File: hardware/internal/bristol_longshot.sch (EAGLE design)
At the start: 39 parts, among them U1 SAM_D20E, U15 BMP180, U2 SI4060, U7 TPS3123, U8 SN74LVC1G32DCKR

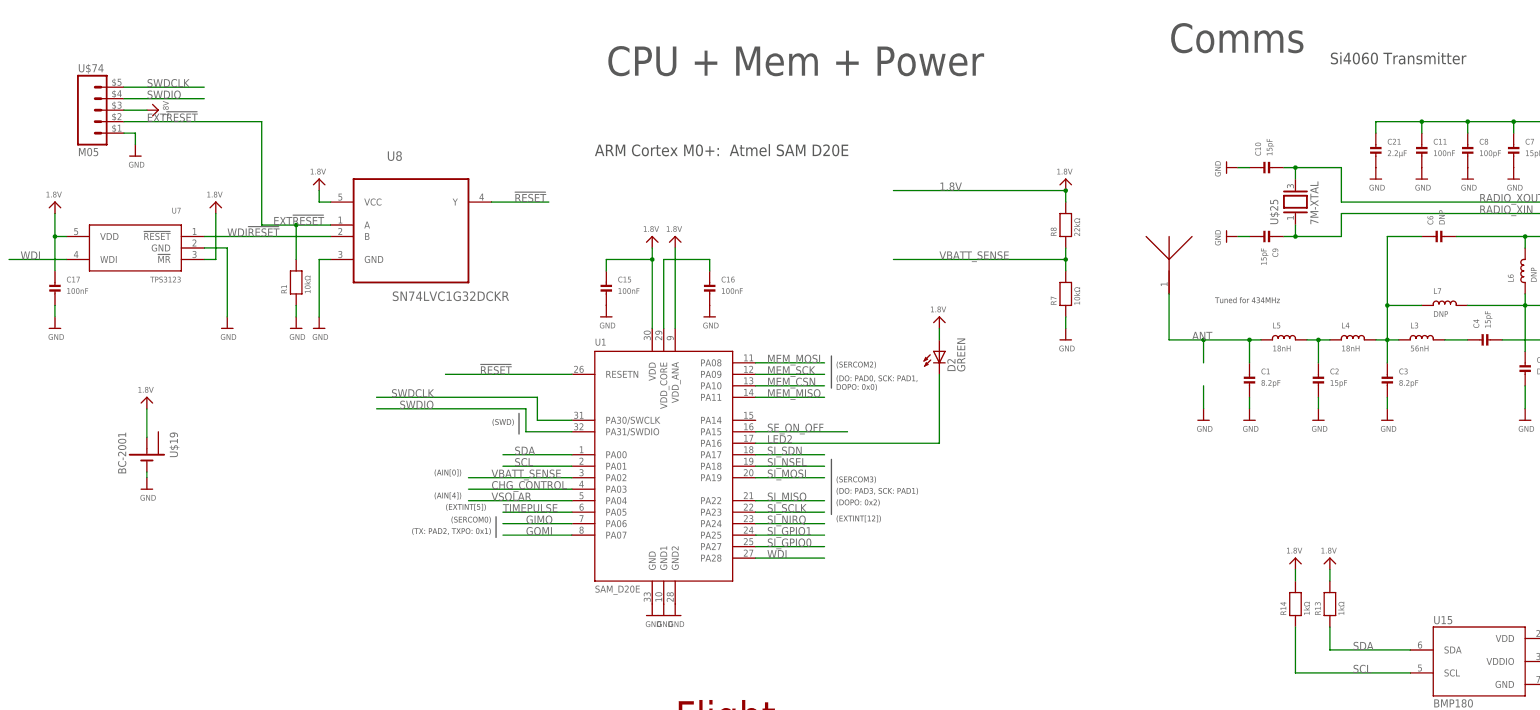
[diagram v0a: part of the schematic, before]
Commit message: Updated main solar active components names to correspond with partslist
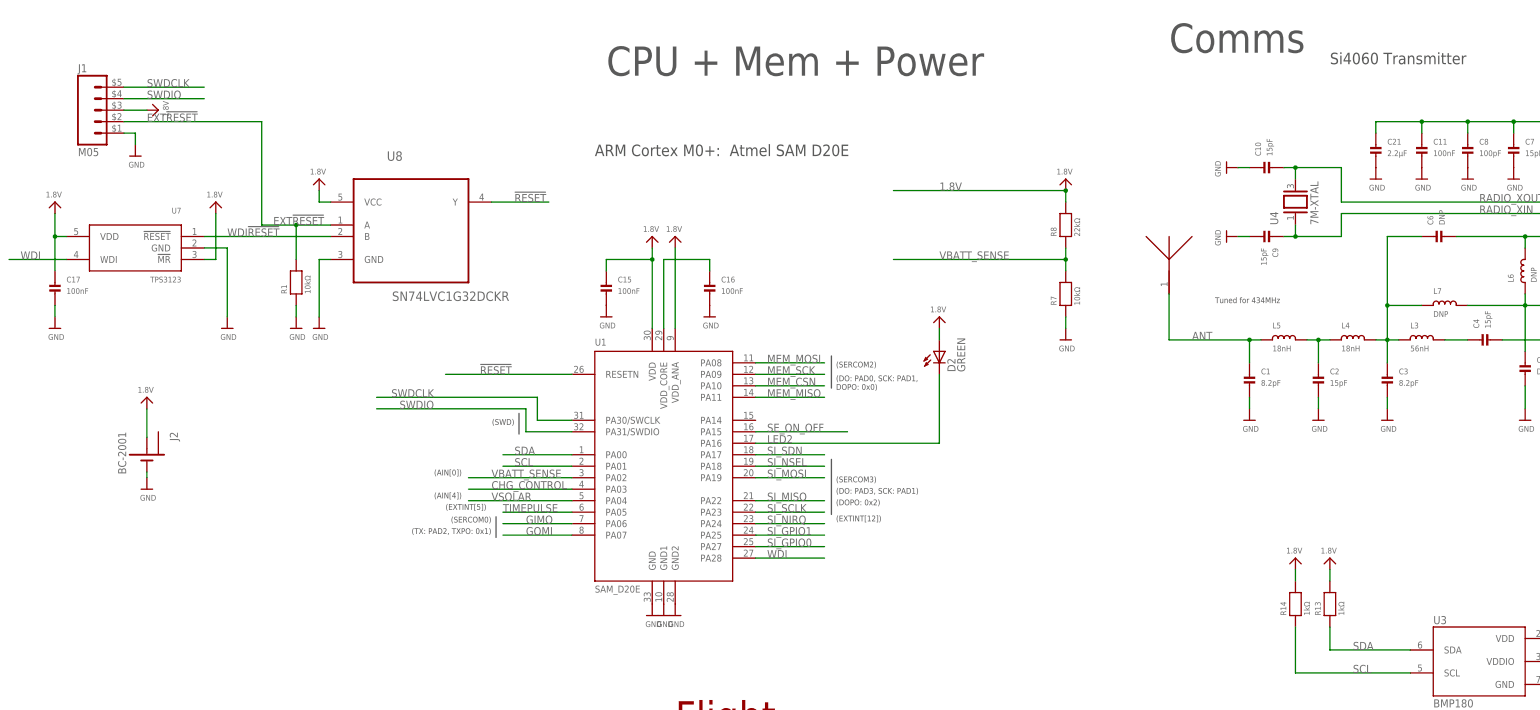
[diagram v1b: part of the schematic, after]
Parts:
- renumbered U$18 to U5, U$19 to J2, U$25 to U4, U$74 to J1, U15 to U3
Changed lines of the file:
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@@
 <part name="U$20" library="microbuilder_v3" deviceset="1.8V" device=""/>
 <part name="U$21" library="microbuilder_v3" deviceset="GND" device=""/>
-<part name="U$31" library="microbuilder_v3" deviceset="GND" device=""/>
 <part name="U8" library="SN74LVC1G32DCKR" deviceset="SN74LVC1G32DCKR" device=""/>
 <part name="U$1" library="microbuilder_v3" deviceset="GND" device=""/>
@@
 <part name="D2" library="led" deviceset="LED" device="CHIPLED_0603" value="GREEN"/>
 <part name="U$73" library="microbuilder_v3" deviceset="1.8V" device=""/>
-<part name="U$74" library="fbri" deviceset="M05" device=""/>
+<part name="J1" library="fbri" deviceset="M05" device=""/>
 <part name="C17" library="microbuilder_v3" deviceset="CAP_CERAMIC" device="_0402" value="100nF"/>
 <part name="U$78" library="microbuilder_v3" deviceset="GND" device=""/>
@@
 <part name="R8" library="microbuilder_v3" deviceset="RESISTOR" device="_0402" value="22kΩ"/>
 <part name="U$56" library="microbuilder_v3" deviceset="GND" device=""/>
-<part name="U15" library="SparkFun-Sensors" deviceset="BMP180" device=""/>
+<part name="U3" library="SparkFun-Sensors" deviceset="BMP180" device=""/>
 <part name="GND13" library="SparkFun" deviceset="GND" device=""/>
 <part name="C24" library="microbuilder_v3" deviceset="CAP_CERAMIC" device="_0402" value="100nF"/>
@@
 <part name="U$16" library="microbuilder_v3" deviceset="1.8V" device=""/>
 <part name="U$17" library="microbuilder_v3" deviceset="1.8V" device=""/>
-<part name="U$18" library="fbri" deviceset="0433AT62A0020E" device=""/>
-<part name="U$19" library="fbri" deviceset="BC-2001" device=""/>
+<part name="U5" library="fbri" deviceset="0433AT62A0020E" device=""/>
+<part name="J2" library="fbri" deviceset="BC-2001" device=""/>
 <part name="U$22" library="microbuilder_v3" deviceset="1.8V" device=""/>
 <part name="U$23" library="microbuilder_v3" deviceset="GND" device=""/>
 <part name="U$24" library="microbuilder_v3" deviceset="1.8V" device=""/>
-<part name="U$25" library="fbri" deviceset="7M-XTAL" device=""/>
+<part name="U4" library="fbri" deviceset="7M-XTAL" device=""/>
 <part name="C9" library="microbuilder_v3" deviceset="CAP_CERAMIC" device="_0402" value="15pF"/>
 <part name="C10" library="microbuilder_v3" deviceset="CAP_CERAMIC" device="_0402" value="15pF"/>
@@
 <instance part="U$20" gate="G$1" x="12.7" y="142.24" rot="MR0"/>
 <instance part="U$21" gate="G$1" x="50.8" y="114.3"/>
-<instance part="U$31" gate="G$1" x="266.7" y="93.98"/>
 <instance part="U8" gate="A" x="91.44" y="139.7"/>
 <instance part="U$1" gate="G$1" x="71.12" y="114.3"/>
@@
 <instance part="D2" gate="G$1" x="208.28" y="109.22"/>
 <instance part="U$73" gate="G$1" x="208.28" y="116.84" rot="MR0"/>
-<instance part="U$74" gate="A" x="22.86" y="162.56"/>
+<instance part="J1" gate="A" x="22.86" y="162.56"/>
 <instance part="C17" gate="G$1" x="12.7" y="121.92"/>
 <instance part="U$78" gate="G$1" x="12.7" y="114.3"/>
@@
 <instance part="R8" gate="G$1" x="236.22" y="137.16" rot="R90"/>
 <instance part="U$56" gate="G$1" x="236.22" y="111.76"/>
-<instance part="U15" gate="G$1" x="327.66" y="40.64"/>
+<instance part="U3" gate="G$1" x="327.66" y="40.64"/>
 <instance part="GND13" gate="1" x="347.98" y="27.94"/>
 <instance part="C24" gate="G$1" x="358.14" y="33.02"/>
@@
 <instance part="U$16" gate="G$1" x="294.64" y="63.5" rot="MR0"/>
 <instance part="U$17" gate="G$1" x="347.98" y="58.42" rot="MR0"/>
-<instance part="U$18" gate="G$1" x="259.08" y="129.54"/>
-<instance part="U$19" gate="G$1" x="33.02" y="86.36" rot="R270"/>
+<instance part="U5" gate="G$1" x="259.08" y="129.54"/>
+<instance part="J2" gate="G$1" x="33.02" y="86.36" rot="R270"/>
 <instance part="U$22" gate="G$1" x="33.02" y="99.06" rot="MR0"/>
 <instance part="U$23" gate="G$1" x="33.02" y="78.74"/>
 <instance part="U$24" gate="G$1" x="236.22" y="147.32" rot="MR0"/>
-<instance part="U$25" gate="G$1" x="287.02" y="142.24" rot="R90"/>
+<instance part="U4" gate="G$1" x="287.02" y="142.24" rot="R90"/>
 <instance part="C9" gate="G$1" x="279.4" y="134.62" rot="R270"/>
 <instance part="C10" gate="G$1" x="281.94" y="149.86" rot="R90"/>
@@
 </segment>
 <segment>
-<pinref part="U$31" gate="G$1" pin="GND"/>
-<wire x1="266.7" y1="96.52" x2="266.7" y2="101.6" width="0.1524" layer="91"/>
-</segment>
-<segment>
 <pinref part="U$1" gate="G$1" pin="GND"/>
 <wire x1="73.66" y1="129.54" x2="71.12" y2="129.54" width="0.1524" layer="91"/>
@@
 </segment>
 <segment>
-<pinref part="U$74" gate="A" pin="1"/>
+<pinref part="J1" gate="A" pin="1"/>
 <wire x1="27.94" y1="157.48" x2="30.48" y2="157.48" width="0.1524" layer="91"/>
 <pinref part="U$6" gate="G$1" pin="GND"/>
@@
 </segment>
 <segment>
-<pinref part="U15" gate="G$1" pin="GND"/>
+<pinref part="U3" gate="G$1" pin="GND"/>
 <pinref part="GND13" gate="1" pin="GND"/>
 <wire x1="342.9" y1="35.56" x2="347.98" y2="35.56" width="0.1524" layer="91"/>
@@
 <segment>
 <pinref part="U$23" gate="G$1" pin="GND"/>
-<pinref part="U$19" gate="G$1" pin="-"/>
+<pinref part="J2" gate="G$1" pin="-"/>
 <wire x1="33.02" y1="81.28" x2="33.02" y2="82.55" width="0.1524" layer="91"/>
 </segment>
@@
 </segment>
 <segment>
-<pinref part="U$74" gate="A" pin="4"/>
+<pinref part="J1" gate="A" pin="4"/>
 <wire x1="27.94" y1="165.1" x2="45.72" y2="165.1" width="0.1524" layer="91"/>
 <label x="33.02" y="165.1" size="1.778" layer="95"/>
@@
 </segment>
 <segment>
-<pinref part="U$74" gate="A" pin="5"/>
+<pinref part="J1" gate="A" pin="5"/>
 <wire x1="27.94" y1="167.64" x2="45.72" y2="167.64" width="0.1524" layer="91"/>
 <label x="33.02" y="167.64" size="1.778" layer="95"/>
@@
 </segment>
 <segment>
-<pinref part="U$74" gate="A" pin="3"/>
+<pinref part="J1" gate="A" pin="3"/>
 <pinref part="U$4" gate="G$1" pin="1.8V"/>
 <wire x1="27.94" y1="162.56" x2="33.02" y2="162.56" width="0.1524" layer="91"/>
@@
 </segment>
 <segment>
-<pinref part="U15" gate="G$1" pin="VDD"/>
+<pinref part="U3" gate="G$1" pin="VDD"/>
 <wire x1="342.9" y1="45.72" x2="347.98" y2="45.72" width="0.1524" layer="91"/>
 <wire x1="347.98" y1="45.72" x2="347.98" y2="55.88" width="0.1524" layer="91"/>
@@
 <wire x1="347.98" y1="45.72" x2="370.84" y2="45.72" width="0.1524" layer="91"/>
 <wire x1="370.84" y1="45.72" x2="370.84" y2="38.1" width="0.1524" layer="91"/>
-<pinref part="U15" gate="G$1" pin="VDDIO"/>
+<pinref part="U3" gate="G$1" pin="VDDIO"/>
 <wire x1="342.9" y1="40.64" x2="347.98" y2="40.64" width="0.1524" layer="91"/>
 <junction x="347.98" y="40.64"/>
@@
 </segment>
 <segment>
-<pinref part="U$19" gate="G$1" pin="+"/>
+<pinref part="J2" gate="G$1" pin="+"/>
 <pinref part="U$22" gate="G$1" pin="1.8V"/>
 <wire x1="33.02" y1="90.17" x2="33.02" y2="96.52" width="0.1524" layer="91"/>
@@
 <wire x1="279.4" y1="111.76" x2="276.86" y2="111.76" width="0.1524" layer="91"/>
 <wire x1="276.86" y1="111.76" x2="276.86" y2="106.68" width="0.1524" layer="91"/>
-<wire x1="259.08" y1="111.76" x2="266.7" y2="111.76" width="0.1524" layer="91"/>
 <label x="264.16" y="111.76" size="1.778" layer="95" ratio="11"/>
 <junction x="276.86" y="111.76"/>
-<wire x1="266.7" y1="111.76" x2="276.86" y2="111.76" width="0.1524" layer="91"/>
-<wire x1="266.7" y1="106.68" x2="266.7" y2="111.76" width="0.1524" layer="91"/>
-<junction x="266.7" y="111.76"/>
-<pinref part="U$18" gate="G$1" pin="P$1"/>
+<wire x1="259.08" y1="111.76" x2="276.86" y2="111.76" width="0.1524" layer="91"/>
+<pinref part="U5" gate="G$1" pin="P$1"/>
 <wire x1="259.08" y1="111.76" x2="259.08" y2="121.92" width="0.1524" layer="91"/>
 </segment>
@@
 <wire x1="350.52" y1="139.7" x2="297.18" y2="139.7" width="0.1524" layer="91"/>
 <wire x1="297.18" y1="139.7" x2="297.18" y2="134.62" width="0.1524" layer="91"/>
-<pinref part="U$25" gate="G$1" pin="1"/>
+<pinref part="U4" gate="G$1" pin="1"/>
 <wire x1="297.18" y1="134.62" x2="287.02" y2="134.62" width="0.1524" layer="91"/>
 <wire x1="287.02" y1="134.62" x2="287.02" y2="137.16" width="0.1524" layer="91"/>
@@
 <junction x="66.04" y="137.16"/>
 <label x="60.96" y="137.16" size="1.778" layer="95"/>
-<pinref part="U$74" gate="A" pin="2"/>
+<pinref part="J1" gate="A" pin="2"/>
 <wire x1="27.94" y1="160.02" x2="58.42" y2="160.02" width="0.1524" layer="91"/>
 <label x="33.02" y="160.02" size="1.778" layer="95"/>
@@
 </segment>
 <segment>
-<pinref part="U15" gate="G$1" pin="SDA"/>
+<pinref part="U3" gate="G$1" pin="SDA"/>
 <wire x1="312.42" y1="43.18" x2="294.64" y2="43.18" width="0.1524" layer="91"/>
 <label x="299.72" y="43.18" size="1.778" layer="95"/>
@@
 </segment>
 <segment>
-<pinref part="U15" gate="G$1" pin="SCL"/>
+<pinref part="U3" gate="G$1" pin="SCL"/>
 <wire x1="312.42" y1="38.1" x2="287.02" y2="38.1" width="0.1524" layer="91"/>
 <label x="299.72" y="38.1" size="1.778" layer="95"/>
@@
 <net name="RADIO_XOUT" class="0">
 <segment>
-<pinref part="U$25" gate="G$1" pin="2"/>
+<pinref part="U4" gate="G$1" pin="2"/>
 <wire x1="287.02" y1="147.32" x2="287.02" y2="149.86" width="0.1524" layer="91"/>
 <wire x1="287.02" y1="149.86" x2="297.18" y2="149.86" width="0.1524" layer="91"/>

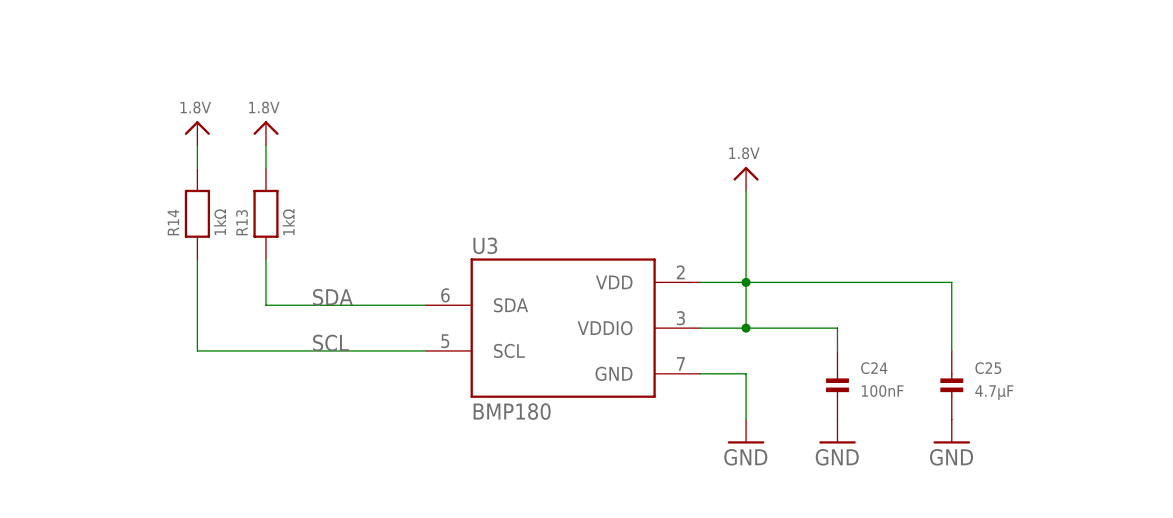
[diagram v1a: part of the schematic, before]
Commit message: Updated many parts lists, updated bard numbering, removed makefiles for inactive things
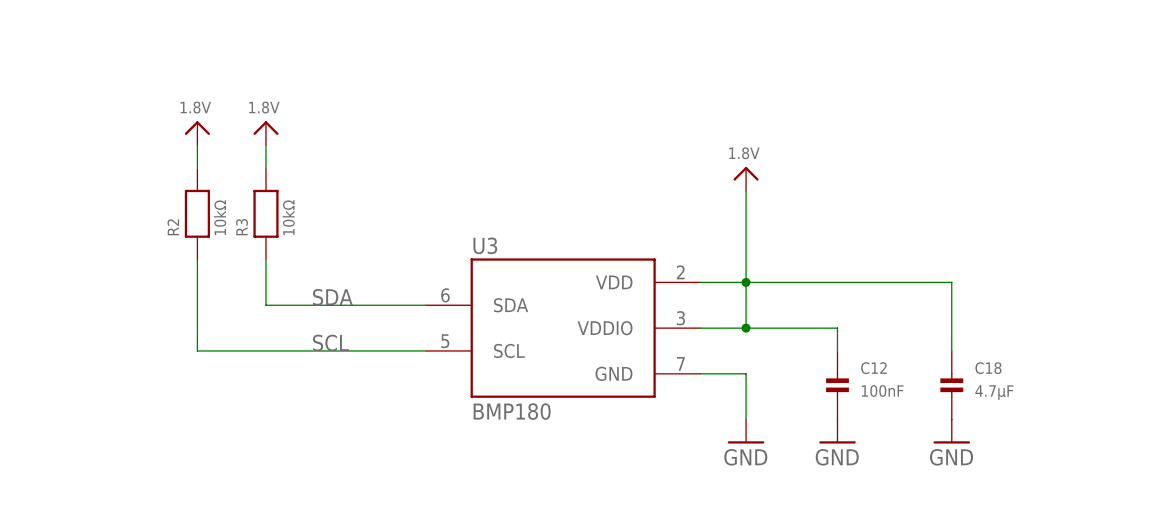
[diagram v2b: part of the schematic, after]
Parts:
- R2, R3: value 1kΩ -> 10kΩ
- renumbered C24 to C12, C25 to C18, R13 to R3, R14 to R2
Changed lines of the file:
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@@
 <part name="U3" library="SparkFun-Sensors" deviceset="BMP180" device=""/>
 <part name="GND13" library="SparkFun" deviceset="GND" device=""/>
-<part name="C24" library="microbuilder_v3" deviceset="CAP_CERAMIC" device="_0402" value="100nF"/>
-<part name="C25" library="microbuilder_v3" deviceset="CAP_CERAMIC" device="_0402" value="4.7µF"/>
+<part name="C12" library="microbuilder_v3" deviceset="CAP_CERAMIC" device="_0402" value="100nF"/>
+<part name="C18" library="microbuilder_v3" deviceset="CAP_CERAMIC" device="_0402" value="4.7µF"/>
 <part name="GND14" library="SparkFun" deviceset="GND" device=""/>
 <part name="GND20" library="SparkFun" deviceset="GND" device=""/>
-<part name="R13" library="microbuilder_v3" deviceset="RESISTOR" device="_0402" value="1kΩ"/>
-<part name="R14" library="microbuilder_v3" deviceset="RESISTOR" device="_0402" value="1kΩ"/>
+<part name="R3" library="microbuilder_v3" deviceset="RESISTOR" device="_0402" value="10kΩ"/>
+<part name="R2" library="microbuilder_v3" deviceset="RESISTOR" device="_0402" value="10kΩ"/>
 <part name="U$3" library="microbuilder_v3" deviceset="1.8V" device=""/>
 <part name="U$16" library="microbuilder_v3" deviceset="1.8V" device=""/>
@@
 <instance part="U3" gate="G$1" x="327.66" y="40.64"/>
 <instance part="GND13" gate="1" x="347.98" y="27.94"/>
-<instance part="C24" gate="G$1" x="358.14" y="33.02"/>
-<instance part="C25" gate="G$1" x="370.84" y="33.02"/>
+<instance part="C12" gate="G$1" x="358.14" y="33.02"/>
+<instance part="C18" gate="G$1" x="370.84" y="33.02"/>
 <instance part="GND14" gate="1" x="358.14" y="27.94"/>
 <instance part="GND20" gate="1" x="370.84" y="27.94"/>
-<instance part="R13" gate="G$1" x="294.64" y="53.34" rot="R90"/>
-<instance part="R14" gate="G$1" x="287.02" y="53.34" rot="R90"/>
+<instance part="R3" gate="G$1" x="294.64" y="53.34" rot="R90"/>
+<instance part="R2" gate="G$1" x="287.02" y="53.34" rot="R90"/>
 <instance part="U$3" gate="G$1" x="287.02" y="63.5" rot="MR0"/>
 <instance part="U$16" gate="G$1" x="294.64" y="63.5" rot="MR0"/>
@@
 </segment>
 <segment>
-<pinref part="C24" gate="G$1" pin="P$2"/>
+<pinref part="C12" gate="G$1" pin="P$2"/>
 <pinref part="GND14" gate="1" pin="GND"/>
 </segment>
 <segment>
-<pinref part="C25" gate="G$1" pin="P$2"/>
+<pinref part="C18" gate="G$1" pin="P$2"/>
 <pinref part="GND20" gate="1" pin="GND"/>
 </segment>
@@
 </segment>
 <segment>
-<pinref part="R14" gate="G$1" pin="2"/>
+<pinref part="R2" gate="G$1" pin="2"/>
 <wire x1="287.02" y1="60.96" x2="287.02" y2="58.42" width="0.1524" layer="91"/>
 <pinref part="U$3" gate="G$1" pin="1.8V"/>
 </segment>
 <segment>
-<pinref part="R13" gate="G$1" pin="2"/>
+<pinref part="R3" gate="G$1" pin="2"/>
 <wire x1="294.64" y1="60.96" x2="294.64" y2="58.42" width="0.1524" layer="91"/>
 <pinref part="U$16" gate="G$1" pin="1.8V"/>
@@
 <wire x1="347.98" y1="40.64" x2="347.98" y2="45.72" width="0.1524" layer="91"/>
 <junction x="347.98" y="45.72"/>
-<pinref part="C24" gate="G$1" pin="P$1"/>
+<pinref part="C12" gate="G$1" pin="P$1"/>
 <wire x1="347.98" y1="40.64" x2="358.14" y2="40.64" width="0.1524" layer="91"/>
 <wire x1="358.14" y1="40.64" x2="358.14" y2="38.1" width="0.1524" layer="91"/>
-<pinref part="C25" gate="G$1" pin="P$1"/>
+<pinref part="C18" gate="G$1" pin="P$1"/>
 <wire x1="347.98" y1="45.72" x2="370.84" y2="45.72" width="0.1524" layer="91"/>
 <wire x1="370.84" y1="45.72" x2="370.84" y2="38.1" width="0.1524" layer="91"/>
@@
 <wire x1="312.42" y1="43.18" x2="294.64" y2="43.18" width="0.1524" layer="91"/>
 <label x="299.72" y="43.18" size="1.778" layer="95"/>
-<pinref part="R13" gate="G$1" pin="1"/>
+<pinref part="R3" gate="G$1" pin="1"/>
 <wire x1="294.64" y1="43.18" x2="294.64" y2="48.26" width="0.1524" layer="91"/>
 </segment>
@@
 <wire x1="312.42" y1="38.1" x2="287.02" y2="38.1" width="0.1524" layer="91"/>
 <label x="299.72" y="38.1" size="1.778" layer="95"/>
-<pinref part="R14" gate="G$1" pin="1"/>
+<pinref part="R2" gate="G$1" pin="1"/>
 <wire x1="287.02" y1="38.1" x2="287.02" y2="48.26" width="0.1524" layer="91"/>
 </segment>
